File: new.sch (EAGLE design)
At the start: 51 parts, among them K1 351, K2 351, K3 351, K4 351, K5 351, K6 351

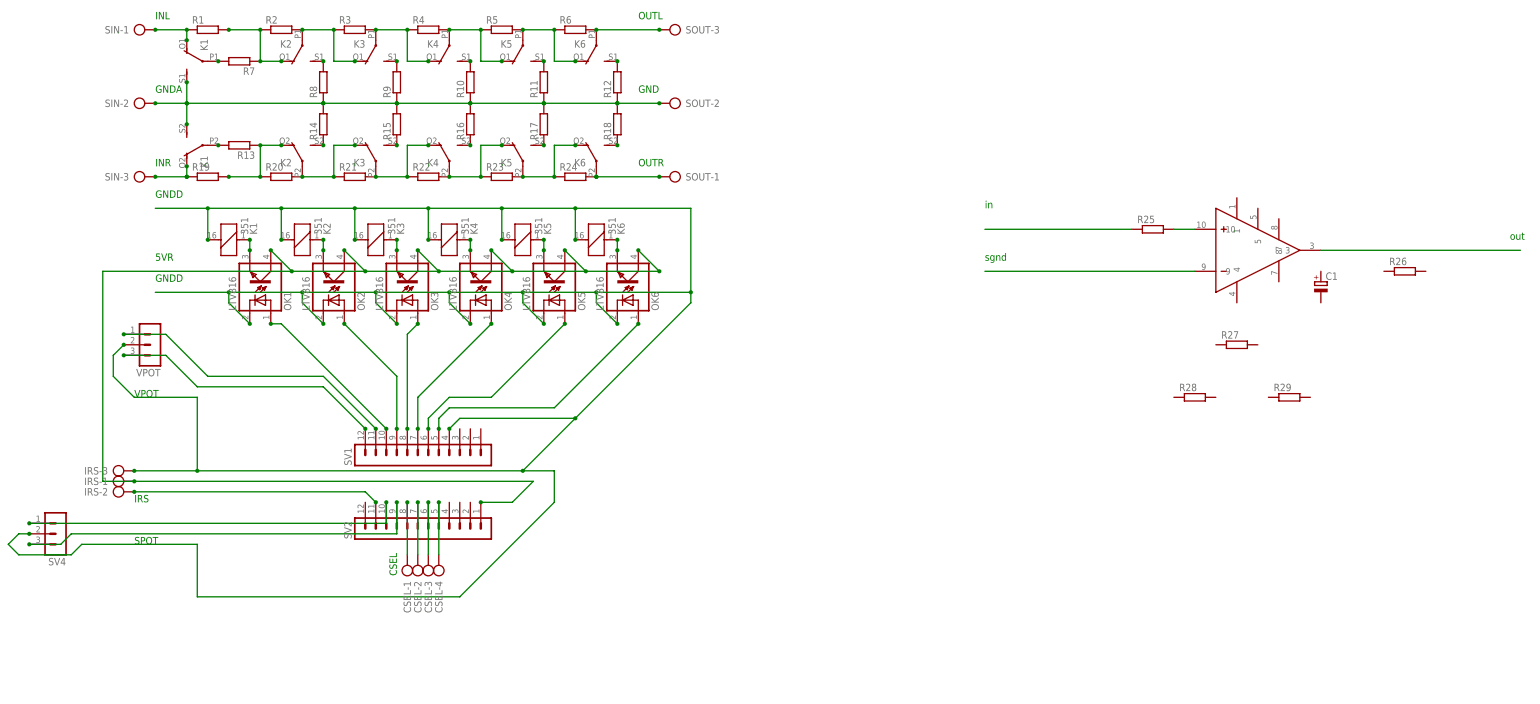
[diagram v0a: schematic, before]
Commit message: Added gainclone to scheme
Need to add control for mute relay
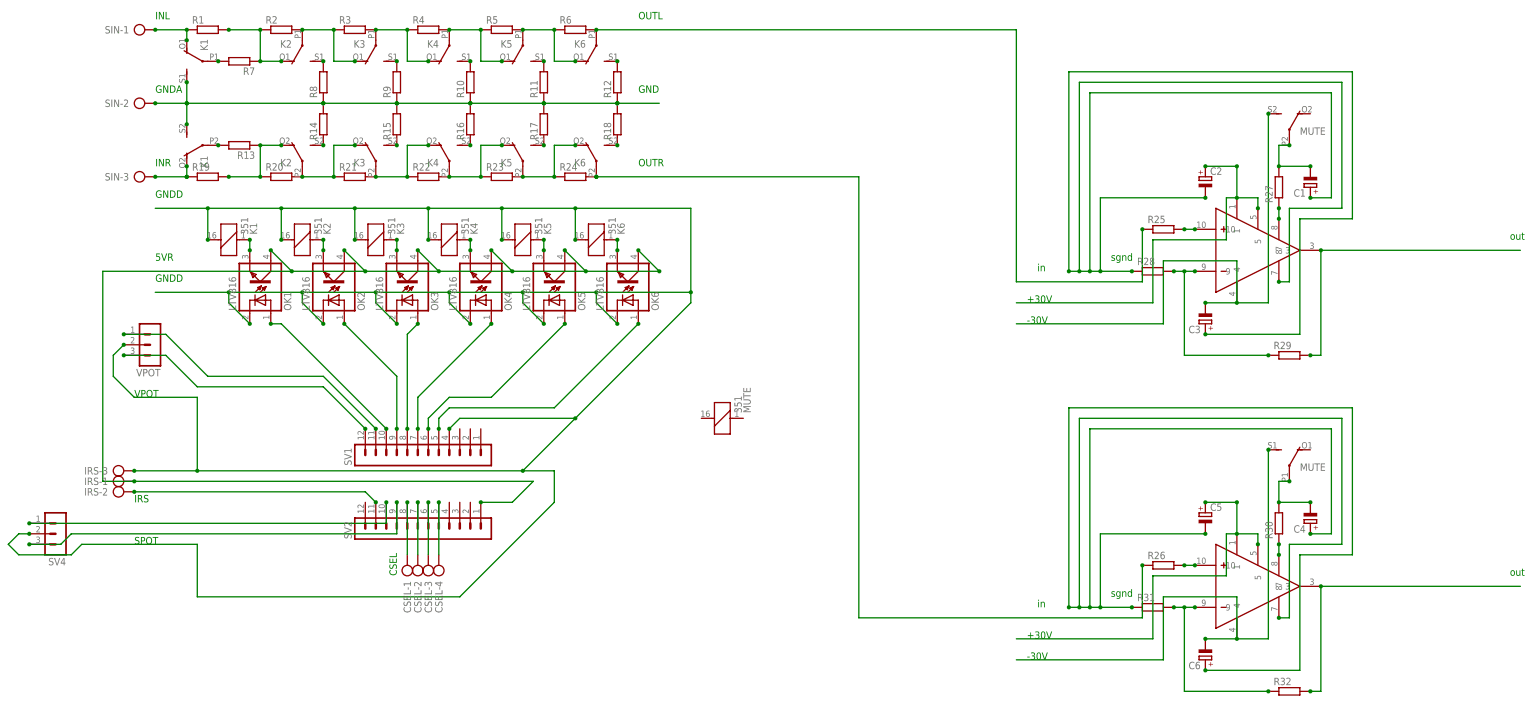
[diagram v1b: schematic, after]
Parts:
- removed SOUT: (no value), con-ptr500:AK500/3
- added C2, C3, C4, C5, C6: (no value), rcl:CPOL-EUE5-13
- added MUTE: 351, relay:351
- added R30, R31, R32: (no value), rcl:R-EU_0207/10
- added U$2: (no value), LM3886:LM3886T
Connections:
- new net N$53: C2.+, U$1.1, U$1.5
- new net N$55: R27.1, U$1.8
- new net N$56: C1.-, MUTE3.P, R27.2
- new net N$57: C3.-, MUTE3.S, U$1.4
- new net N$58: R26.2, U$2.10
- new net N$60: R32.2, U$2.3
- new net N$61: C5.+, U$2.1, U$2.5
- new net N$62: R31.2, R32.1, U$2.9
- new net N$64: R30.1, U$2.8
- new net N$65: C4.-, MUTE2.P, R30.2
- net GNDA: now also C1.+, C2.-, C3.+, C4.+, C5.-, C6.+, R28.1, R31.1, U$1.7, U$2.7; no longer SOUT-2.KL
- net N$32: now also R26.1; no longer SOUT-1.KL
- net N$48: now also C6.-, MUTE2.S, U$2.4; no longer R25.1
- net N$51: now also R28.2, R29.1
- net N$52: now also R29.2
- net N$6: now also R25.1; no longer SOUT-3.KL
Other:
- note added: "+30V"
- note added: "-30V"
- moved on the sheet: C1, R25, R26, R27, R28, R29
